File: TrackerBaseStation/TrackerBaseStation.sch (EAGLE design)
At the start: 22 parts, among them Q1 16MHz, U1 ATMEGA8U2MU, U2 RCLAMP0502A, U3 NRF24L01NOPAD, U4 BD2425NNRF0404, X1 USB-LEG

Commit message: pin header for base station
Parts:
- added J1: DF12A3.0-14DS, adjacent-reality:DF12A3.0-14DS
- added R5: 10k, SparkFun-Passives:RESISTOR0402-RES
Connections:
- removed net N$14: U1.PB1(SCK), U3.SCK
- removed net N$15: U1.PB2(MOSI), U3.MOSI
- removed net N$16: U1.PB3(MISO), U3.MISO
- new net ANT: L1.2
- new net MISO: J1.1, U1.PB3(MISO), U3.MISO
- new net MOSI: J1.4, U1.PB2(MOSI), U3.MOSI
- new net PD0: J1.9, U1.PD0
- new net PD1: J1.10, U1.PD1
- new net PD4: J1.11, U1.PD4
- new net PD5: J1.12, U1.PD5
- new net PD6: J1.13, U1.PD6(RTS)
- new net PD7: J1.14, U1.PD7(CTS)
- new net RESET: J1.5, R5.1, U1.RESET/PC1
- new net RX: J1.7, U1.PD2(RX)
- new net SCK: J1.3, U1.PB1(SCK), U3.SCK
- new net TX: J1.8, U1.PD3(TX)
- net +3V3: now also J1.2, R5.2
- net CE: now also U1.PB5; no longer U1.PD7(CTS)
- net GND: now also J1.6
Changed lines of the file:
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@@
 <part name="C10" library="SparkFun-Passives" deviceset="CAP" device="0402-CAP" value="100nF"/>
 <part name="X1" library="adjacent-reality" deviceset="USB" device="-LEG"/>
+<part name="J1" library="adjacent-reality" deviceset="DF12A3.0-14DS" device=""/>
+<part name="R5" library="SparkFun-Passives" deviceset="RESISTOR" device="0402-RES" value="10k"/>
+<part name="+3V4" library="supply1" deviceset="+3V3" device=""/>
+<part name="GND4" library="supply1" deviceset="GND" device=""/>
 </parts>
 <sheets>
@@
 <instance part="+3V1" gate="G$1" x="180.34" y="160.02"/>
 <instance part="+3V2" gate="G$1" x="210.82" y="83.82"/>
-<instance part="+3V3" gate="G$1" x="93.98" y="127"/>
+<instance part="+3V3" gate="G$1" x="93.98" y="132.08"/>
 <instance part="GND3" gate="1" x="60.96" y="99.06"/>
 <instance part="C8" gate="G$1" x="55.88" y="104.14"/>
@@
 <instance part="C10" gate="G$1" x="55.88" y="53.34"/>
 <instance part="X1" gate="G$1" x="17.78" y="91.44" rot="R180"/>
+<instance part="J1" gate="G$1" x="119.38" y="154.94"/>
+<instance part="R5" gate="G$1" x="99.06" y="119.38" rot="R90"/>
+<instance part="+3V4" gate="G$1" x="139.7" y="170.18"/>
+<instance part="GND4" gate="1" x="139.7" y="149.86"/>
 </instances>
 <busses>
@@
 <junction x="60.96" y="101.6"/>
 </segment>
-</net>
-<net name="N$14" class="0">
+<segment>
+<pinref part="J1" gate="G$1" pin="6"/>
+<pinref part="GND4" gate="1" pin="GND"/>
+<wire x1="127" y1="157.48" x2="139.7" y2="157.48" width="0.1524" layer="91"/>
+<wire x1="139.7" y1="157.48" x2="139.7" y2="152.4" width="0.1524" layer="91"/>
+</segment>
+</net>
+<net name="SCK" class="0">
 <segment>
 <pinref part="U1" gate="G$1" pin="PB1(SCK)"/>
@@
 <pinref part="U3" gate="G$1" pin="SCK"/>
 <wire x1="147.32" y1="132.08" x2="157.48" y2="132.08" width="0.1524" layer="91"/>
-</segment>
-</net>
-<net name="N$15" class="0">
+<label x="142.24" y="104.14" size="1.778" layer="95"/>
+</segment>
+<segment>
+<pinref part="J1" gate="G$1" pin="3"/>
+<wire x1="111.76" y1="160.02" x2="109.22" y2="160.02" width="0.1524" layer="91"/>
+<label x="109.22" y="160.02" size="1.778" layer="95" rot="MR0"/>
+</segment>
+</net>
+<net name="MOSI" class="0">
 <segment>
 <pinref part="U1" gate="G$1" pin="PB2(MOSI)"/>
@@
 <pinref part="U3" gate="G$1" pin="MOSI"/>
 <wire x1="149.86" y1="129.54" x2="157.48" y2="129.54" width="0.1524" layer="91"/>
-</segment>
-</net>
-<net name="N$16" class="0">
+<label x="142.24" y="101.6" size="1.778" layer="95"/>
+</segment>
+<segment>
+<pinref part="J1" gate="G$1" pin="4"/>
+<wire x1="127" y1="160.02" x2="129.54" y2="160.02" width="0.1524" layer="91"/>
+<label x="129.54" y="160.02" size="1.778" layer="95"/>
+</segment>
+</net>
+<net name="MISO" class="0">
 <segment>
 <pinref part="U1" gate="G$1" pin="PB3(MISO)"/>
@@
 <pinref part="U3" gate="G$1" pin="MISO"/>
 <wire x1="152.4" y1="127" x2="157.48" y2="127" width="0.1524" layer="91"/>
+<label x="142.24" y="99.06" size="1.778" layer="95"/>
+</segment>
+<segment>
+<pinref part="J1" gate="G$1" pin="1"/>
+<wire x1="111.76" y1="162.56" x2="109.22" y2="162.56" width="0.1524" layer="91"/>
+<label x="109.22" y="162.56" size="1.778" layer="95" rot="MR0"/>
 </segment>
 </net>
@@
 <net name="CE" class="0">
 <segment>
-<pinref part="U1" gate="G$1" pin="PD7(CTS)"/>
-<wire x1="139.7" y1="50.8" x2="142.24" y2="50.8" width="0.1524" layer="91"/>
-<label x="142.24" y="50.8" size="1.778" layer="95"/>
-</segment>
-<segment>
 <pinref part="U3" gate="G$1" pin="CE"/>
 <wire x1="157.48" y1="137.16" x2="154.94" y2="137.16" width="0.1524" layer="91"/>
 <label x="154.94" y="137.16" size="1.778" layer="95" rot="MR0"/>
+</segment>
+<segment>
+<pinref part="U1" gate="G$1" pin="PB5"/>
+<wire x1="139.7" y1="93.98" x2="142.24" y2="93.98" width="0.1524" layer="91"/>
+<label x="142.24" y="93.98" size="1.778" layer="95"/>
 </segment>
 </net>
@@
 <junction x="93.98" y="58.42"/>
 <pinref part="+3V3" gate="G$1" pin="+3V3"/>
-<wire x1="93.98" y1="124.46" x2="93.98" y2="109.22" width="0.1524" layer="91"/>
+<wire x1="93.98" y1="129.54" x2="93.98" y2="124.46" width="0.1524" layer="91"/>
 <junction x="93.98" y="101.6"/>
 <pinref part="C8" gate="G$1" pin="1"/>
-<wire x1="93.98" y1="106.68" x2="93.98" y2="101.6" width="0.1524" layer="91"/>
+<wire x1="93.98" y1="124.46" x2="93.98" y2="109.22" width="0.1524" layer="91"/>
+<wire x1="93.98" y1="109.22" x2="93.98" y2="101.6" width="0.1524" layer="91"/>
 <wire x1="55.88" y1="109.22" x2="66.04" y2="109.22" width="0.1524" layer="91"/>
 <wire x1="66.04" y1="106.68" x2="66.04" y2="109.22" width="0.1524" layer="91"/>
 <wire x1="66.04" y1="109.22" x2="93.98" y2="109.22" width="0.1524" layer="91"/>
-<wire x1="93.98" y1="109.22" x2="93.98" y2="106.68" width="0.1524" layer="91"/>
 <junction x="66.04" y="109.22"/>
+<pinref part="R5" gate="G$1" pin="2"/>
+<wire x1="99.06" y1="124.46" x2="93.98" y2="124.46" width="0.1524" layer="91"/>
+<junction x="93.98" y="124.46"/>
 </segment>
 <segment>
@@
 <wire x1="180.34" y1="157.48" x2="180.34" y2="149.86" width="0.1524" layer="91"/>
 </segment>
+<segment>
+<pinref part="J1" gate="G$1" pin="2"/>
+<pinref part="+3V4" gate="G$1" pin="+3V3"/>
+<wire x1="127" y1="162.56" x2="139.7" y2="162.56" width="0.1524" layer="91"/>
+<wire x1="139.7" y1="162.56" x2="139.7" y2="167.64" width="0.1524" layer="91"/>
+</segment>
 </net>
 <net name="N$6" class="0">
@@
 </segment>
 </net>
+<net name="RESET" class="0">
+<segment>
+<pinref part="R5" gate="G$1" pin="1"/>
+<pinref part="U1" gate="G$1" pin="RESET/PC1"/>
+<wire x1="99.06" y1="114.3" x2="99.06" y2="106.68" width="0.1524" layer="91"/>
+<label x="99.06" y="111.76" size="1.778" layer="95"/>
+</segment>
+<segment>
+<pinref part="J1" gate="G$1" pin="5"/>
+<wire x1="111.76" y1="157.48" x2="109.22" y2="157.48" width="0.1524" layer="91"/>
+<label x="109.22" y="157.48" size="1.778" layer="95" rot="MR0"/>
+</segment>
+</net>
+<net name="RX" class="0">
+<segment>
+<pinref part="J1" gate="G$1" pin="7"/>
+<wire x1="111.76" y1="154.94" x2="109.22" y2="154.94" width="0.1524" layer="91"/>
+<label x="109.22" y="154.94" size="1.778" layer="95" rot="MR0"/>
+</segment>
+<segment>
+<pinref part="U1" gate="G$1" pin="PD2(RX)"/>
+<wire x1="139.7" y1="63.5" x2="142.24" y2="63.5" width="0.1524" layer="91"/>
+<label x="142.24" y="63.5" size="1.778" layer="95"/>
+</segment>
+</net>
+<net name="TX" class="0">
+<segment>
+<pinref part="J1" gate="G$1" pin="8"/>
+<wire x1="127" y1="154.94" x2="129.54" y2="154.94" width="0.1524" layer="91"/>
+<label x="129.54" y="154.94" size="1.778" layer="95"/>
+</segment>
+<segment>
+<pinref part="U1" gate="G$1" pin="PD3(TX)"/>
+<wire x1="139.7" y1="60.96" x2="142.24" y2="60.96" width="0.1524" layer="91"/>
+<label x="142.24" y="60.96" size="1.778" layer="95"/>
+</segment>
+</net>
+<net name="PD0" class="0">
+<segment>
+<pinref part="U1" gate="G$1" pin="PD0"/>
+<wire x1="139.7" y1="68.58" x2="142.24" y2="68.58" width="0.1524" layer="91"/>
+<label x="142.24" y="68.58" size="1.778" layer="95"/>
+</segment>
+<segment>
+<pinref part="J1" gate="G$1" pin="9"/>
+<wire x1="111.76" y1="152.4" x2="109.22" y2="152.4" width="0.1524" layer="91"/>
+<label x="109.22" y="152.4" size="1.778" layer="95" rot="MR0"/>
+</segment>
+</net>
+<net name="PD1" class="0">
+<segment>
+<pinref part="U1" gate="G$1" pin="PD1"/>
+<wire x1="139.7" y1="66.04" x2="142.24" y2="66.04" width="0.1524" layer="91"/>
+<label x="142.24" y="66.04" size="1.778" layer="95"/>
+</segment>
+<segment>
+<pinref part="J1" gate="G$1" pin="10"/>
+<wire x1="127" y1="152.4" x2="129.54" y2="152.4" width="0.1524" layer="91"/>
+<label x="129.54" y="152.4" size="1.778" layer="95"/>
+</segment>
+</net>
+<net name="PD4" class="0">
+<segment>
+<pinref part="U1" gate="G$1" pin="PD4"/>
+<wire x1="139.7" y1="58.42" x2="142.24" y2="58.42" width="0.1524" layer="91"/>
+<label x="142.24" y="58.42" size="1.778" layer="95"/>
+</segment>
+<segment>
+<pinref part="J1" gate="G$1" pin="11"/>
+<wire x1="111.76" y1="149.86" x2="109.22" y2="149.86" width="0.1524" layer="91"/>
+<label x="109.22" y="149.86" size="1.778" layer="95" rot="MR0"/>
+</segment>
+</net>
+<net name="PD5" class="0">
+<segment>
+<pinref part="U1" gate="G$1" pin="PD5"/>
+<wire x1="139.7" y1="55.88" x2="142.24" y2="55.88" width="0.1524" layer="91"/>
+<label x="142.24" y="55.88" size="1.778" layer="95"/>
+</segment>
+<segment>
+<pinref part="J1" gate="G$1" pin="12"/>
+<wire x1="127" y1="149.86" x2="129.54" y2="149.86" width="0.1524" layer="91"/>
+<label x="129.54" y="149.86" size="1.778" layer="95"/>
+</segment>
+</net>
+<net name="PD6" class="0">
+<segment>
+<pinref part="U1" gate="G$1" pin="PD6(RTS)"/>
+<wire x1="139.7" y1="53.34" x2="142.24" y2="53.34" width="0.1524" layer="91"/>
+<label x="142.24" y="53.34" size="1.778" layer="95"/>
+</segment>
+<segment>
+<pinref part="J1" gate="G$1" pin="13"/>
+<wire x1="111.76" y1="147.32" x2="109.22" y2="147.32" width="0.1524" layer="91"/>
+<label x="109.22" y="147.32" size="1.778" layer="95" rot="MR0"/>
+</segment>
+</net>
+<net name="PD7" class="0">
+<segment>
+<pinref part="U1" gate="G$1" pin="PD7(CTS)"/>
+<wire x1="139.7" y1="50.8" x2="142.24" y2="50.8" width="0.1524" layer="91"/>
+<label x="142.24" y="50.8" size="1.778" layer="95"/>
+</segment>
+<segment>
+<pinref part="J1" gate="G$1" pin="14"/>
+<wire x1="127" y1="147.32" x2="129.54" y2="147.32" width="0.1524" layer="91"/>
+<label x="129.54" y="147.32" size="1.778" layer="95"/>
+</segment>
+</net>
+<net name="ANT" class="0">
+<segment>
+<pinref part="L1" gate="G$1" pin="2"/>
+<wire x1="251.46" y1="134.62" x2="256.54" y2="134.62" width="0.1524" layer="91"/>
+<wire x1="256.54" y1="134.62" x2="256.54" y2="147.32" width="0.1524" layer="91"/>
+<label x="256.54" y="147.32" size="1.778" layer="95"/>
+</segment>
+</net>

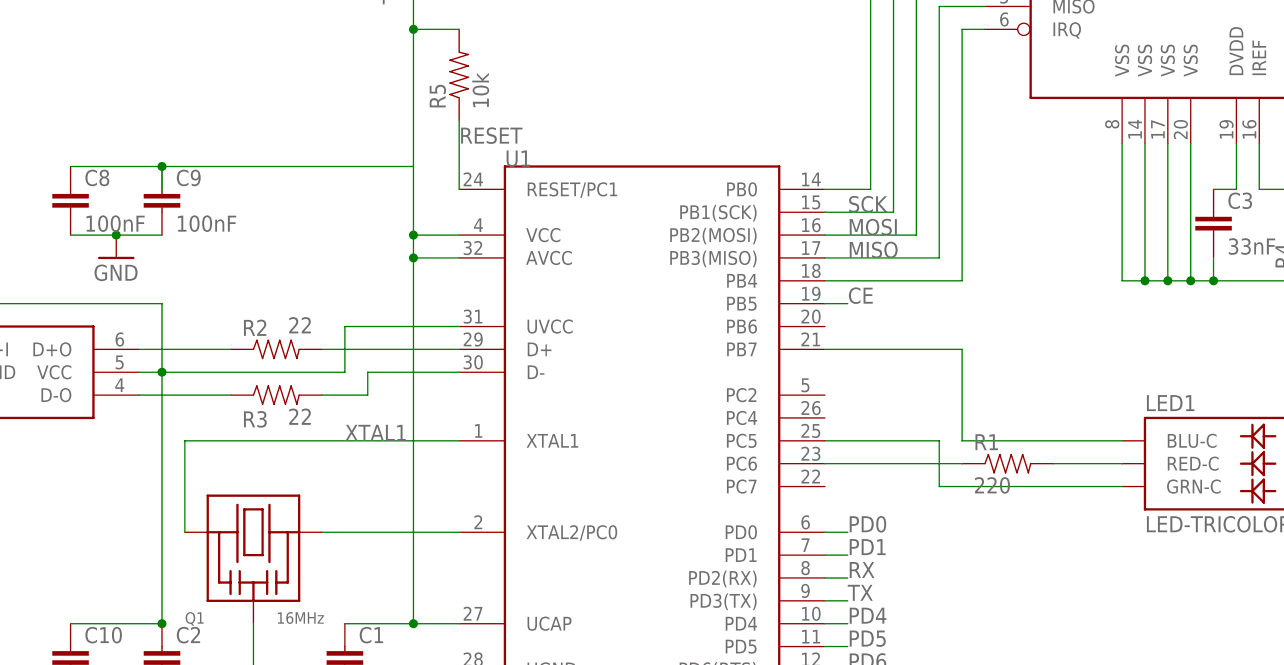
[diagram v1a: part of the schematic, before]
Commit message: start of base station layout
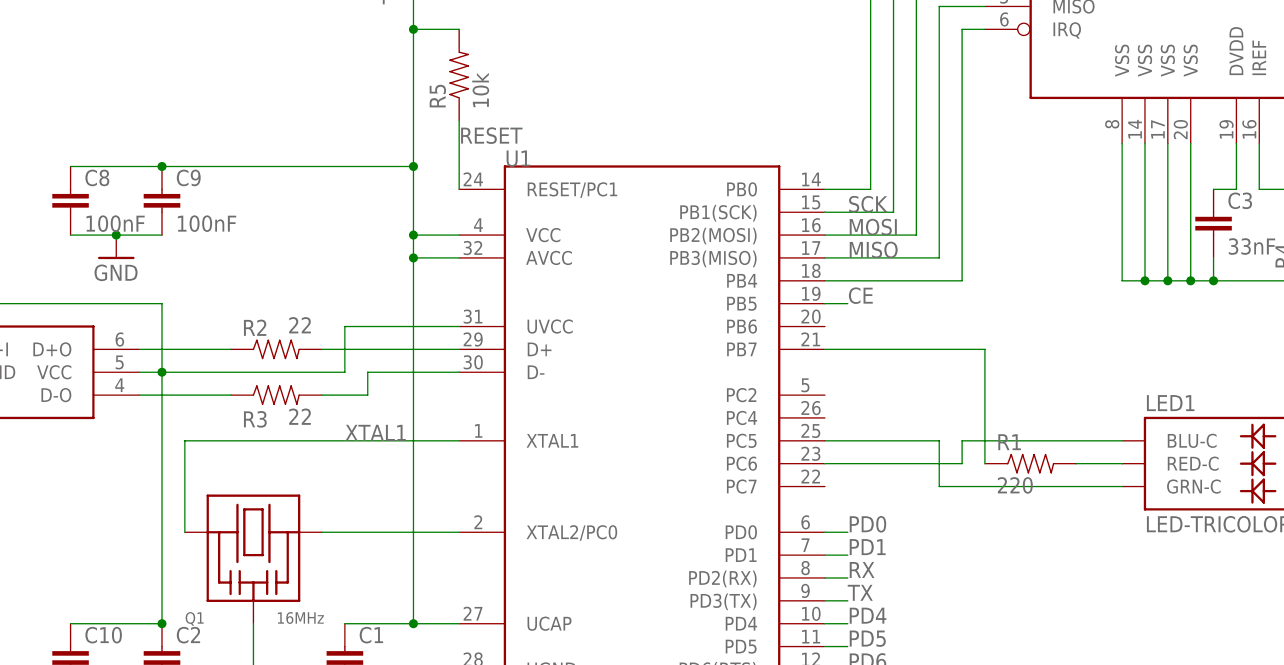
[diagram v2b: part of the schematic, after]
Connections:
- net +3V3: now also C9.1
- net N$1: now also U1.PC6; no longer U1.PB7
- net N$3: now also U1.PB7; no longer U1.PC6
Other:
- moved on the sheet: R1
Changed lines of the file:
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@@
 <instance part="U4" gate="G$1" x="223.52" y="132.08"/>
 <instance part="U3" gate="G$1" x="180.34" y="129.54"/>
-<instance part="R1" gate="G$1" x="160.02" y="76.2"/>
+<instance part="R1" gate="G$1" x="162.56" y="76.2"/>
 <instance part="R2" gate="G$1" x="78.74" y="88.9" smashed="yes">
 <attribute name="NAME" x="74.93" y="90.3986" size="1.778" layer="95"/>
@@
 <pinref part="LED1" gate="G$1" pin="BLU-C"/>
 <wire x1="172.72" y1="78.74" x2="154.94" y2="78.74" width="0.1524" layer="91"/>
-<wire x1="154.94" y1="78.74" x2="154.94" y2="88.9" width="0.1524" layer="91"/>
-<pinref part="U1" gate="G$1" pin="PB7"/>
-<wire x1="154.94" y1="88.9" x2="139.7" y2="88.9" width="0.1524" layer="91"/>
+<wire x1="154.94" y1="78.74" x2="154.94" y2="76.2" width="0.1524" layer="91"/>
+<pinref part="U1" gate="G$1" pin="PC6"/>
+<wire x1="154.94" y1="76.2" x2="139.7" y2="76.2" width="0.1524" layer="91"/>
 </segment>
 </net>
@@
 <pinref part="LED1" gate="G$1" pin="RED-C"/>
 <pinref part="R1" gate="G$1" pin="2"/>
-<wire x1="172.72" y1="76.2" x2="165.1" y2="76.2" width="0.1524" layer="91"/>
-</segment>
-</net>
-<net name="N$3" class="0">
-<segment>
-<pinref part="R1" gate="G$1" pin="1"/>
-<wire x1="154.94" y1="76.2" x2="139.7" y2="76.2" width="0.1524" layer="91"/>
-<pinref part="U1" gate="G$1" pin="PC6"/>
+<wire x1="172.72" y1="76.2" x2="167.64" y2="76.2" width="0.1524" layer="91"/>
 </segment>
 </net>
@@
 <wire x1="93.98" y1="129.54" x2="93.98" y2="124.46" width="0.1524" layer="91"/>
 <junction x="93.98" y="101.6"/>
+<wire x1="93.98" y1="124.46" x2="93.98" y2="109.22" width="0.1524" layer="91"/>
+<pinref part="R5" gate="G$1" pin="2"/>
+<wire x1="93.98" y1="109.22" x2="93.98" y2="101.6" width="0.1524" layer="91"/>
+<wire x1="99.06" y1="124.46" x2="93.98" y2="124.46" width="0.1524" layer="91"/>
+<junction x="93.98" y="124.46"/>
 <pinref part="C8" gate="G$1" pin="1"/>
-<wire x1="93.98" y1="124.46" x2="93.98" y2="109.22" width="0.1524" layer="91"/>
-<wire x1="93.98" y1="109.22" x2="93.98" y2="101.6" width="0.1524" layer="91"/>
+<pinref part="C9" gate="G$1" pin="1"/>
 <wire x1="55.88" y1="109.22" x2="66.04" y2="109.22" width="0.1524" layer="91"/>
-<wire x1="66.04" y1="106.68" x2="66.04" y2="109.22" width="0.1524" layer="91"/>
 <wire x1="66.04" y1="109.22" x2="93.98" y2="109.22" width="0.1524" layer="91"/>
 <junction x="66.04" y="109.22"/>
-<pinref part="R5" gate="G$1" pin="2"/>
-<wire x1="99.06" y1="124.46" x2="93.98" y2="124.46" width="0.1524" layer="91"/>
-<junction x="93.98" y="124.46"/>
+<junction x="93.98" y="109.22"/>
 </segment>
 <segment>
@@
 </segment>
 </net>
+<net name="N$3" class="0">
+<segment>
+<pinref part="R1" gate="G$1" pin="1"/>
+<wire x1="157.48" y1="76.2" x2="157.48" y2="88.9" width="0.1524" layer="91"/>
+<pinref part="U1" gate="G$1" pin="PB7"/>
+<wire x1="157.48" y1="88.9" x2="139.7" y2="88.9" width="0.1524" layer="91"/>
+</segment>
+</net>
 </nets>
 </sheet>
 </sheets>
+<errors>
+</errors>
 </schematic>
 </drawing>

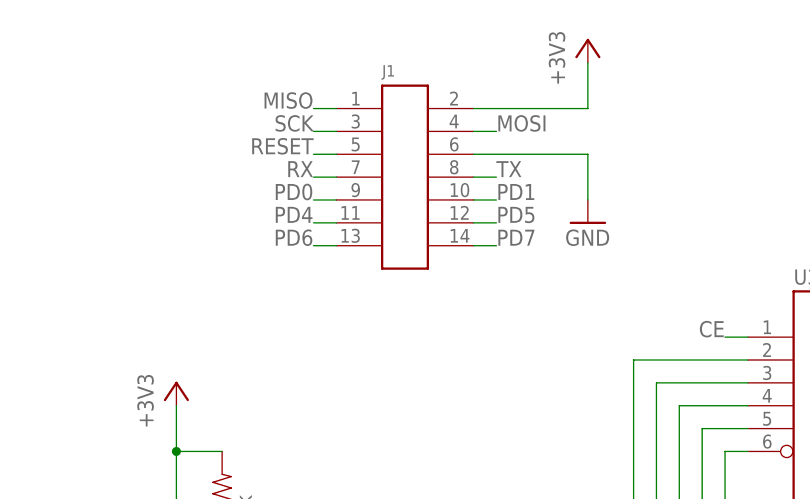
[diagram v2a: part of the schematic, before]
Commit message: with antenna
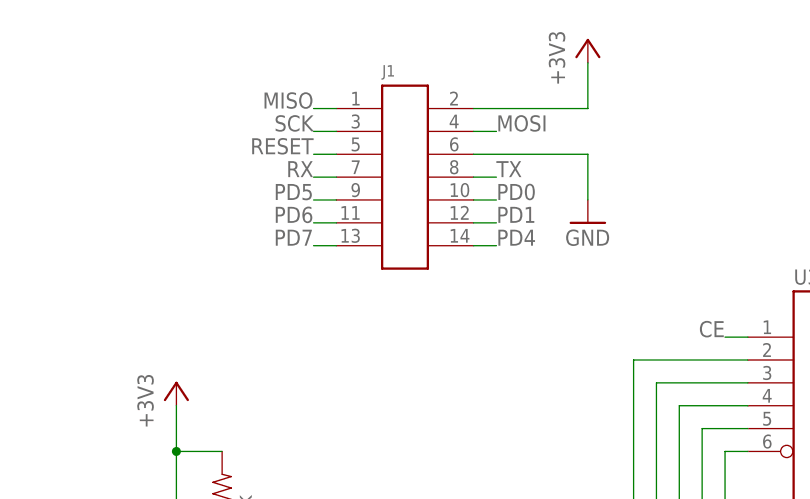
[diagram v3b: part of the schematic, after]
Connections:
- net PD0: now also J1.10; no longer J1.9
- net PD1: now also J1.12; no longer J1.10
- net PD4: now also J1.14; no longer J1.11
- net PD5: now also J1.9; no longer J1.12
- net PD6: now also J1.11; no longer J1.13
- net PD7: now also J1.13; no longer J1.14
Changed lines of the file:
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@@
 </segment>
 <segment>
-<pinref part="J1" gate="G$1" pin="9"/>
-<wire x1="111.76" y1="152.4" x2="109.22" y2="152.4" width="0.1524" layer="91"/>
-<label x="109.22" y="152.4" size="1.778" layer="95" rot="MR0"/>
+<pinref part="J1" gate="G$1" pin="10"/>
+<wire x1="127" y1="152.4" x2="129.54" y2="152.4" width="0.1524" layer="91"/>
+<label x="129.54" y="152.4" size="1.778" layer="95"/>
 </segment>
 </net>
@@
 </segment>
 <segment>
-<pinref part="J1" gate="G$1" pin="10"/>
-<wire x1="127" y1="152.4" x2="129.54" y2="152.4" width="0.1524" layer="91"/>
-<label x="129.54" y="152.4" size="1.778" layer="95"/>
+<pinref part="J1" gate="G$1" pin="12"/>
+<wire x1="127" y1="149.86" x2="129.54" y2="149.86" width="0.1524" layer="91"/>
+<label x="129.54" y="149.86" size="1.778" layer="95"/>
 </segment>
 </net>
@@
 </segment>
 <segment>
-<pinref part="J1" gate="G$1" pin="11"/>
-<wire x1="111.76" y1="149.86" x2="109.22" y2="149.86" width="0.1524" layer="91"/>
-<label x="109.22" y="149.86" size="1.778" layer="95" rot="MR0"/>
+<pinref part="J1" gate="G$1" pin="14"/>
+<wire x1="127" y1="147.32" x2="129.54" y2="147.32" width="0.1524" layer="91"/>
+<label x="129.54" y="147.32" size="1.778" layer="95"/>
 </segment>
 </net>
@@
 </segment>
 <segment>
-<pinref part="J1" gate="G$1" pin="12"/>
-<wire x1="127" y1="149.86" x2="129.54" y2="149.86" width="0.1524" layer="91"/>
-<label x="129.54" y="149.86" size="1.778" layer="95"/>
+<pinref part="J1" gate="G$1" pin="9"/>
+<wire x1="111.76" y1="152.4" x2="109.22" y2="152.4" width="0.1524" layer="91"/>
+<label x="109.22" y="152.4" size="1.778" layer="95" rot="MR0"/>
 </segment>
 </net>
@@
 </segment>
 <segment>
-<pinref part="J1" gate="G$1" pin="13"/>
-<wire x1="111.76" y1="147.32" x2="109.22" y2="147.32" width="0.1524" layer="91"/>
-<label x="109.22" y="147.32" size="1.778" layer="95" rot="MR0"/>
+<pinref part="J1" gate="G$1" pin="11"/>
+<wire x1="111.76" y1="149.86" x2="109.22" y2="149.86" width="0.1524" layer="91"/>
+<label x="109.22" y="149.86" size="1.778" layer="95" rot="MR0"/>
 </segment>
 </net>
@@
 </segment>
 <segment>
-<pinref part="J1" gate="G$1" pin="14"/>
-<wire x1="127" y1="147.32" x2="129.54" y2="147.32" width="0.1524" layer="91"/>
-<label x="129.54" y="147.32" size="1.778" layer="95"/>
+<pinref part="J1" gate="G$1" pin="13"/>
+<wire x1="111.76" y1="147.32" x2="109.22" y2="147.32" width="0.1524" layer="91"/>
+<label x="109.22" y="147.32" size="1.778" layer="95" rot="MR0"/>
 </segment>
 </net>
